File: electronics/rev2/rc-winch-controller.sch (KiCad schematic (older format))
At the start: 13 parts, among them J1 Conn_01x06, J2 Conn_01x06, SW1 SETUP, U1 ME6209A33M3G, U2 LPC812M101JDH20, U3 RZ7889

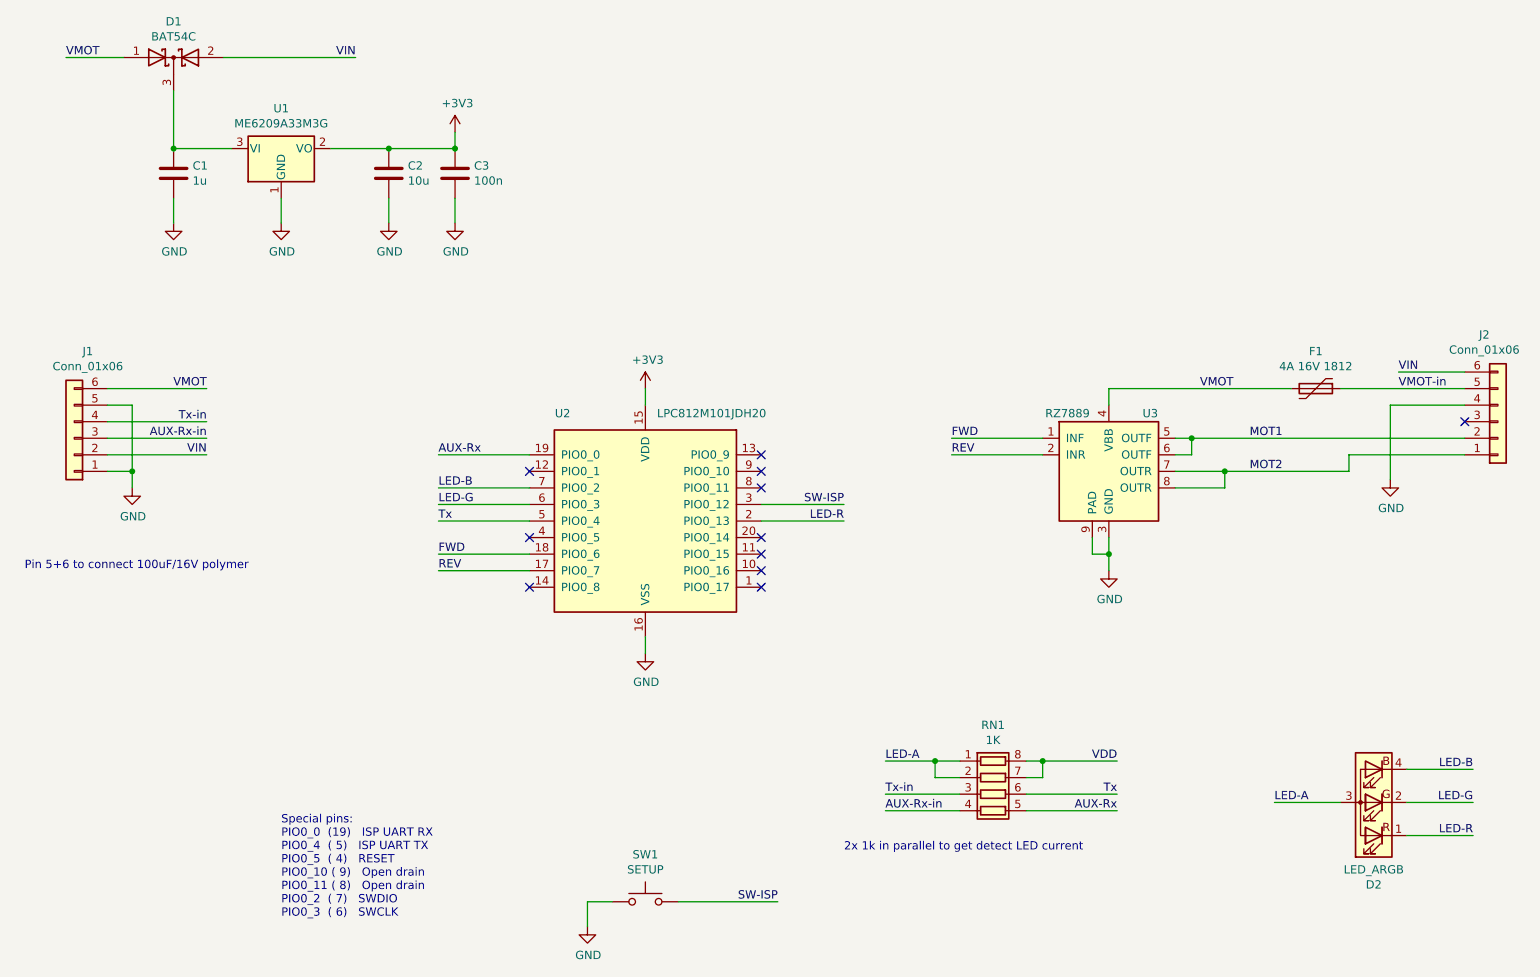
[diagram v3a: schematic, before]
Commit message: Fix LED footprint and current limiting resistor
1k is enough for red and green.
It is a bit dark for blue, but 500R is too bright
for red and green.
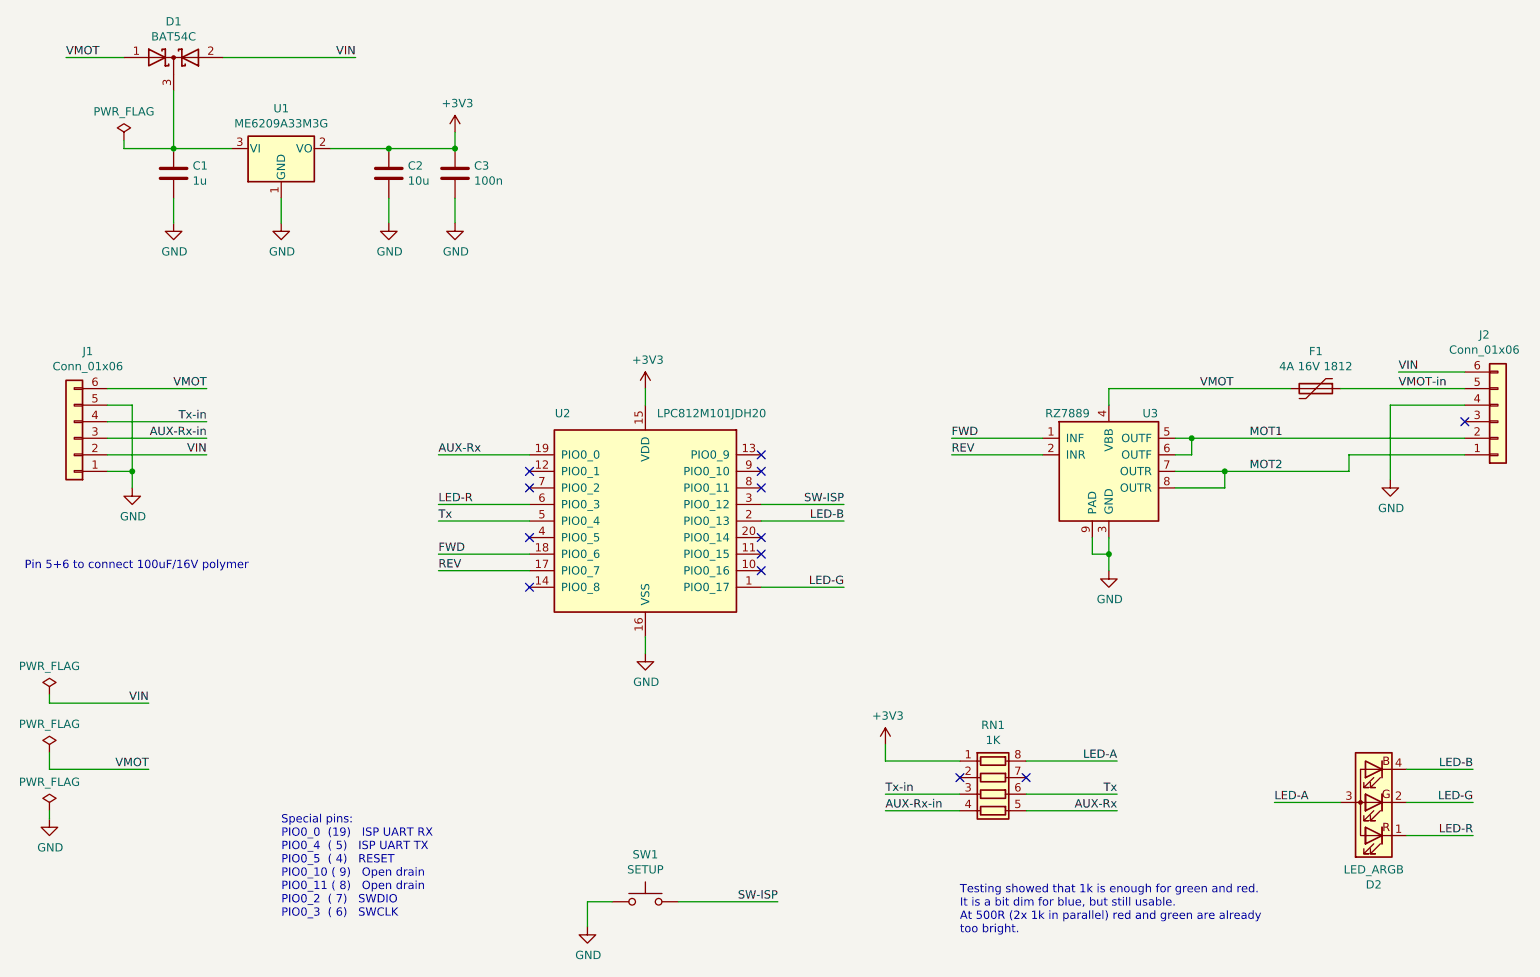
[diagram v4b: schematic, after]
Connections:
- net +3V3: now also RN1.1 (R1.1)
- net LED-A: now also RN1.8 (R1.2); no longer RN1.1 (R1.1), RN1.2 (R2.1)
- net LED-B: now also U2.2 (PIO0_13); no longer U2.7 (PIO0_2)
- net LED-G: now also U2.1 (PIO0_17); no longer U2.6 (PIO0_3)
- net LED-R: now also U2.6 (PIO0_3); no longer U2.2 (PIO0_13)
- net VDD: no longer names the net of RN1.7 (R2.2)
- net VDD: no longer RN1.8 (R1.2)
- no-connect marks 11 -> 13
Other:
- note added: "Testing showed that 1k is enough for green and red.\nIt is a bit dim for blue, but still usable.\nAt 500R (2x 1k in parallel) red and green are already\ntoo bright."
- note removed: "2x 1k in parallel to get detect LED current"
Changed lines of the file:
@@
 	1    0    0    1
 $EndComp
-Wire Wire Line
-	6500 5200 6350 5200
-Wire Wire Line
-	6900 5200 7000 5200
 $Comp
 L power:GND #PWR06
@@
 Wire Wire Line
 	7400 3950 7400 4050
-Text Label 6050 5200 0    50   ~ 0
+Text Label 7450 5200 2    50   ~ 0
 LED-A
 Wire Wire Line
@@
 Text Label 9600 5250 2    50   ~ 0
 LED-B
-Text Label 7450 5200 2    50   ~ 0
-VDD
 Text Label 6050 5500 0    50   ~ 0
 AUX-Rx-in
@@
 Text Label 9150 2950 0    50   ~ 0
 VMOT-in
-Text Notes 5800 5750 0    50   ~ 0
-2x 1k in parallel to get detect LED current
+Text Notes 6500 6250 0    50   ~ 0
+Testing showed that 1k is enough for green and red.\nIt is a bit dim for blue, but still usable.\nAt 500R (2x 1k in parallel) red and green are already\ntoo bright.
 Wire Wire Line
 	7800 3350 7900 3350
@@
 LED-A
 Wire Wire Line
-	6350 5300 6500 5300
-Wire Wire Line
 	6050 5500 6500 5500
-Wire Wire Line
-	7000 5300 6900 5300
 Wire Wire Line
 	6900 5500 7450 5500
@@
 Pin 5+6 to connect 100uF/16V polymer
 Wire Wire Line
-	6350 5200 6350 5300
-Connection ~ 6350 5200
-Wire Wire Line
-	6350 5200 6050 5200
-Wire Wire Line
 	6050 5400 6500 5400
 Wire Wire Line
-	7000 5300 7000 5200
-Connection ~ 7000 5200
-Wire Wire Line
-	7000 5200 7450 5200
-Wire Wire Line
 	6900 5400 7450 5400
 Wire Wire Line
@@
 	8850 3350 9550 3350
 $Comp
-L power:+3V3 #PWR?
+L power:+3V3 #PWR0101
 U 1 1 60252048
 P 3450 1400
-F 0 "#PWR?" H 3450 1250 50  0001 C CNN
+F 0 "#PWR0101" H 3450 1250 50  0001 C CNN
 F 1 "+3V3" H 3465 1573 50  0000 C CNN
 F 2 "" H 3450 1400 50  0001 C CNN
@@
 $EndComp
 $Comp
-L power:+3V3 #PWR?
+L power:+3V3 #PWR0102
 U 1 1 6026DDF4
 P 4600 2950
-F 0 "#PWR?" H 4600 2800 50  0001 C CNN
+F 0 "#PWR0102" H 4600 2800 50  0001 C CNN
 F 1 "+3V3" H 4615 3123 50  0000 C CNN
 F 2 "" H 4600 2950 50  0001 C CNN
@@
 	4600 2950 4600 3050
 $Comp
-L power:GND #PWR?
+L power:GND #PWR0103
 U 1 1 6026FF95
 P 4600 4550
-F 0 "#PWR?" H 4600 4300 50  0001 C CNN
+F 0 "#PWR0103" H 4600 4300 50  0001 C CNN
 F 1 "GND" H 4605 4377 50  0000 C CNN
 F 2 "" H 4600 4550 50  0001 C CNN
@@
 Wire Wire Line
 	3900 3650 3350 3650
-Wire Wire Line
-	3350 3550 3900 3550
-Text Label 3350 3650 0    50   ~ 0
+Text Label 5800 4150 2    50   ~ 0
 LED-G
-Text Label 3350 3550 0    50   ~ 0
+Text Label 5800 3750 2    50   ~ 0
 LED-B
 Wire Wire Line
@@
 Text Label 5800 3650 2    50   ~ 0
 SW-ISP
-Text Label 5800 3750 2    50   ~ 0
+Text Label 3350 3650 0    50   ~ 0
 LED-R
 Wire Wire Line
@@
 NoConn ~ 5300 3950
 NoConn ~ 5300 4050
-NoConn ~ 5300 4150
+Wire Wire Line
+	6050 5200 6500 5200
+Wire Wire Line
+	6900 5200 7450 5200
+NoConn ~ 6900 5300
+NoConn ~ 6500 5300
+$Comp
+L power:+3V3 #PWR0104
+U 1 1 602765C7
+P 6050 5100
+F 0 "#PWR0104" H 6050 4950 50  0001 C CNN
+F 1 "+3V3" H 6065 5273 50  0000 C CNN
+F 2 "" H 6050 5100 50  0001 C CNN
+F 3 "" H 6050 5100 50  0001 C CNN
+	1    6050 5100
+	1    0    0    -1
+$EndComp
+$Comp
+L power:PWR_FLAG #FLG0101
+U 1 1 6027C6ED
+P 1000 4800
+F 0 "#FLG0101" H 1000 4875 50  0001 C CNN
+F 1 "PWR_FLAG" H 1000 4973 50  0000 C CNN
+F 2 "" H 1000 4800 50  0001 C CNN
+F 3 "~" H 1000 4800 50  0001 C CNN
+	1    1000 4800
+	1    0    0    -1
+$EndComp
+$Comp
+L power:PWR_FLAG #FLG0102
+U 1 1 6027C935
+P 1000 5150
+F 0 "#FLG0102" H 1000 5225 50  0001 C CNN
+F 1 "PWR_FLAG" H 1000 5323 50  0000 C CNN
+F 2 "" H 1000 5150 50  0001 C CNN
+F 3 "~" H 1000 5150 50  0001 C CNN
+	1    1000 5150
+	1    0    0    -1
+$EndComp
+Wire Wire Line
+	1000 4800 1000 4850
+Wire Wire Line
+	1000 4850 1600 4850
+Wire Wire Line
+	1000 5150 1000 5250
+Wire Wire Line
+	1000 5250 1600 5250
+Text Label 1600 4850 2    50   ~ 0
+VIN
+Text Label 1600 5250 2    50   ~ 0
+VMOT
+$Comp
+L power:GND #PWR0105
+U 1 1 602850D6
+P 1000 5550
+F 0 "#PWR0105" H 1000 5300 50  0001 C CNN
+F 1 "GND" H 1005 5377 50  0000 C CNN
+F 2 "" H 1000 5550 50  0001 C CNN
+F 3 "" H 1000 5550 50  0001 C CNN
+	1    1000 5550
+	1    0    0    -1
+$EndComp
+$Comp
+L power:PWR_FLAG #FLG0103
+U 1 1 602853CA
+P 1000 5500
+F 0 "#FLG0103" H 1000 5575 50  0001 C CNN
+F 1 "PWR_FLAG" H 1000 5673 50  0000 C CNN
+F 2 "" H 1000 5500 50  0001 C CNN
+F 3 "~" H 1000 5500 50  0001 C CNN
+	1    1000 5500
+	1    0    0    -1
+$EndComp
+Wire Wire Line
+	1000 5500 1000 5550
+$Comp
+L power:PWR_FLAG #FLG0104
+U 1 1 6028AC6C
+P 1450 1450
+F 0 "#FLG0104" H 1450 1525 50  0001 C CNN
+F 1 "PWR_FLAG" H 1450 1623 50  0000 C CNN
+F 2 "" H 1450 1450 50  0001 C CNN
+F 3 "~" H 1450 1450 50  0001 C CNN
+	1    1450 1450
+	1    0    0    -1
+$EndComp
+Wire Wire Line
+	1450 1450 1450 1500
+Wire Wire Line
+	1450 1500 1750 1500
+Wire Wire Line
+	5800 4150 5300 4150
+NoConn ~ 3900 3550
+Wire Wire Line
+	6050 5100 6050 5200
 $EndSCHEMATC

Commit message: Improve layout
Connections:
- net +3V3: now also RN1.7 (R2.2), RN1.8 (R1.2); no longer RN1.1 (R1.1)
- net LED-A: now also RN1.1 (R1.1); no longer RN1.8 (R1.2)
- no-connect marks 13 -> 12
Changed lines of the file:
@@
 Wire Wire Line
 	7400 3950 7400 4050
-Text Label 7450 5200 2    50   ~ 0
+Text Label 6050 5200 0    50   ~ 0
 LED-A
 Wire Wire Line
@@
 	6050 5200 6500 5200
 Wire Wire Line
-	6900 5200 7450 5200
-NoConn ~ 6900 5300
+	6900 5200 7050 5200
 NoConn ~ 6500 5300
 $Comp
 L power:+3V3 #PWR0104
 U 1 1 602765C7
-P 6050 5100
-F 0 "#PWR0104" H 6050 4950 50  0001 C CNN
-F 1 "+3V3" H 6065 5273 50  0000 C CNN
-F 2 "" H 6050 5100 50  0001 C CNN
-F 3 "" H 6050 5100 50  0001 C CNN
-	1    6050 5100
+P 7450 5100
+F 0 "#PWR0104" H 7450 4950 50  0001 C CNN
+F 1 "+3V3" H 7465 5273 50  0000 C CNN
+F 2 "" H 7450 5100 50  0001 C CNN
+F 3 "" H 7450 5100 50  0001 C CNN
+	1    7450 5100
 	1    0    0    -1
 $EndComp
@@
 NoConn ~ 3900 3550
 Wire Wire Line
-	6050 5100 6050 5200
+	7450 5100 7450 5200
+Wire Wire Line
+	6900 5300 7050 5300
+Wire Wire Line
+	7050 5300 7050 5200
+Connection ~ 7050 5200
+Wire Wire Line
+	7050 5200 7450 5200
 $EndSCHEMATC
